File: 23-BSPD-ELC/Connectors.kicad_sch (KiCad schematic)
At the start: 11 parts, among them J1 Conn_02x06_Counter_Clockwise

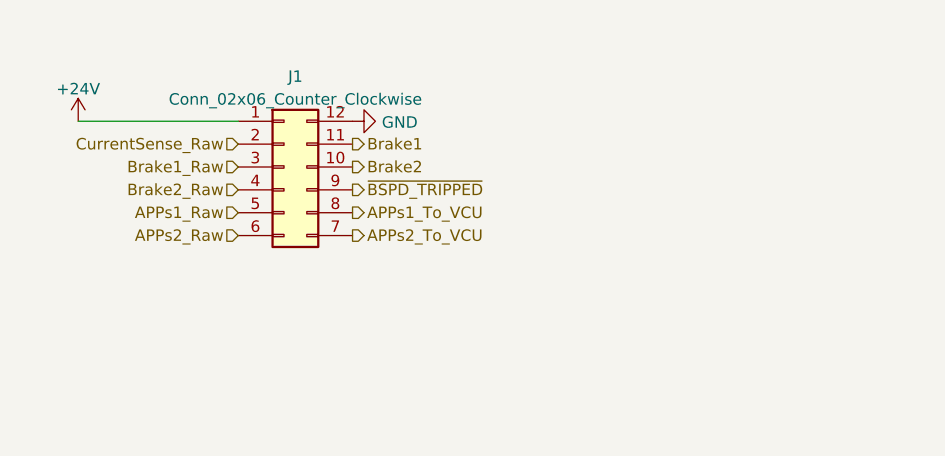
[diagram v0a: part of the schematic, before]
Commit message: Updated connectors and added ~brake signal to vcu
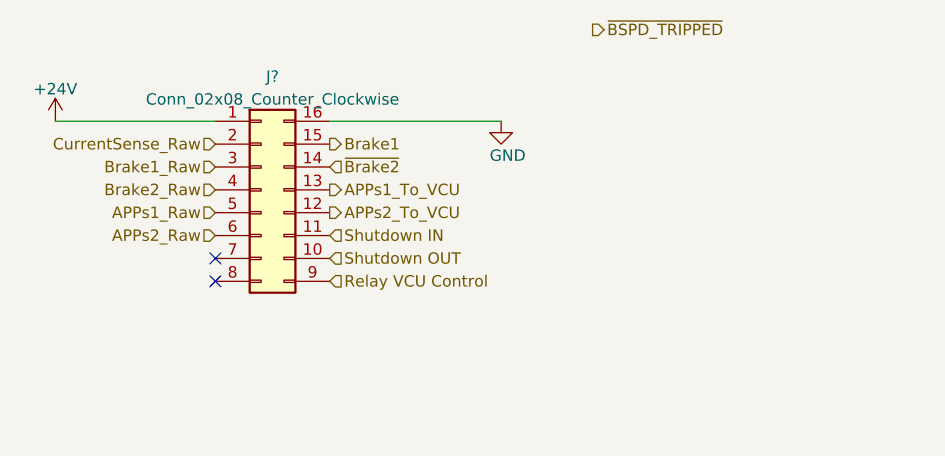
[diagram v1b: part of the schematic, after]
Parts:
- removed J1: Conn_02x06_Counter_Clockwise, symbol Connector_Generic:Conn_02x06_Counter_Clockwise
- added J?: Conn_02x08_Counter_Clockwise, symbol Connector_Generic:Conn_02x08_Counter_Clockwise
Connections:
- net +24V: now also J?.1 (Pin_1)
- net APPs1_Raw: now also J?.5 (Pin_5)
- net APPs1_To_VCU: now also J?.13 (Pin_13)
- net APPs2_Raw: now also J?.6 (Pin_6)
- net APPs2_To_VCU: now also J?.12 (Pin_12)
- net Brake1: now also J?.15 (Pin_15)
- net Brake1_Raw: now also J?.3 (Pin_3)
- net Brake2_Raw: now also J?.4 (Pin_4)
- net CurrentSense_Raw: now also J?.2 (Pin_2)
- net GND: now also J?.16 (Pin_16)
- new net Relay VCU Control: J?.9 (Pin_9)
- new net Shutdown IN: J?.11 (Pin_11)
- new net Shutdown OUT: J?.10 (Pin_10)
- new net ~{Brake2}: J?.14 (Pin_14)
- no-connect marks 4 -> 6
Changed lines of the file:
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@@
   (junction (at 187.96 88.9) (diameter 0) (color 0 0 0 0)
   )
+  (no_connect (at 67.31 100.33))
+  (no_connect (at 67.31 102.87))
   (no_connect (at 193.04 91.44))
   (no_connect (at 231.14 96.52))
@@
     (stroke (width 0) (type default) (color 0 0 0 0))
   )
+  (wire (pts (xy 80.01 85.09) (xy 99.06 85.09))
+    (stroke (width 0) (type default) (color 0 0 0 0))
+  )
   (wire (pts (xy 237.49 91.44) (xy 252.73 91.44))
     (stroke (width 0) (type default) (color 0 0 0 0))
@@
     (stroke (width 0) (type default) (color 0 0 0 0))
   )
-  (wire (pts (xy 52.07 85.09) (xy 69.85 85.09))
+  (wire (pts (xy 49.53 85.09) (xy 67.31 85.09))
     (stroke (width 0) (type default) (color 0 0 0 0))
   )
@@
     (stroke (width 0) (type default) (color 0 0 0 0))
   )
-  (hierarchical_label "APPs1_Raw" (shape input) (at 69.85 95.25 180)
-    (effects (font (size 1.27 1.27)) (justify right))
-  )
-  (hierarchical_label "Brake1_Raw" (shape input) (at 69.85 90.17 180)
-    (effects (font (size 1.27 1.27)) (justify right))
-  )
-  (hierarchical_label "APPs2_Raw" (shape input) (at 69.85 97.79 180)
-    (effects (font (size 1.27 1.27)) (justify right))
-  )
-  (hierarchical_label "Brake2" (shape output) (at 82.55 90.17 0)
-    (effects (font (size 1.27 1.27)) (justify left))
+  (hierarchical_label "APPs1_Raw" (shape input) (at 67.31 95.25 180)
+    (effects (font (size 1.27 1.27)) (justify right))
+  )
+  (hierarchical_label "Shutdown OUT" (shape input) (at 80.01 100.33 0)
+    (effects (font (size 1.27 1.27)) (justify left))
+  )
+  (hierarchical_label "Relay VCU Control" (shape input) (at 80.01 102.87 0)
+    (effects (font (size 1.27 1.27)) (justify left))
+  )
+  (hierarchical_label "Brake1_Raw" (shape input) (at 67.31 90.17 180)
+    (effects (font (size 1.27 1.27)) (justify right))
+  )
+  (hierarchical_label "APPs2_Raw" (shape input) (at 67.31 97.79 180)
+    (effects (font (size 1.27 1.27)) (justify right))
   )
   (hierarchical_label "Brake2_Raw" (shape input) (at 190.5 120.65 0)
@@
     (effects (font (size 1.27 1.27)) (justify left))
   )
-  (hierarchical_label "APPs1_To_VCU" (shape output) (at 82.55 95.25 0)
-    (effects (font (size 1.27 1.27)) (justify left))
-  )
-  (hierarchical_label "APPs2_To_VCU" (shape output) (at 82.55 97.79 0)
-    (effects (font (size 1.27 1.27)) (justify left))
-  )
-  (hierarchical_label "~{BSPD_TRIPPED}" (shape output) (at 82.55 92.71 0)
-    (effects (font (size 1.27 1.27)) (justify left))
-  )
-  (hierarchical_label "Brake1" (shape output) (at 82.55 87.63 0)
-    (effects (font (size 1.27 1.27)) (justify left))
-  )
-  (hierarchical_label "CurrentSense_Raw" (shape input) (at 69.85 87.63 180)
-    (effects (font (size 1.27 1.27)) (justify right))
-  )
-  (hierarchical_label "Brake2_Raw" (shape input) (at 69.85 92.71 180)
-    (effects (font (size 1.27 1.27)) (justify right))
-  )
-  (symbol (lib_id "power:GND") (at 82.55 85.09 90) (mirror x) (unit 1)
-    (in_bom yes) (on_board yes)
-    (property "Reference" "#PWR02" (id 0) (at 88.9 85.09 0)
-      (effects (font (size 1.27 1.27)) hide)
-    )
-    (property "Value" "GND" (id 1) (at 85.8012 85.217 90)
+  (hierarchical_label "APPs1_To_VCU" (shape output) (at 80.01 92.71 0)
+    (effects (font (size 1.27 1.27)) (justify left))
+  )
+  (hierarchical_label "APPs2_To_VCU" (shape output) (at 80.01 95.25 0)
+    (effects (font (size 1.27 1.27)) (justify left))
+  )
+  (hierarchical_label "~{BSPD_TRIPPED}" (shape output) (at 109.22 74.93 0)
+    (effects (font (size 1.27 1.27)) (justify left))
+  )
+  (hierarchical_label "Shutdown IN" (shape input) (at 80.01 97.79 0)
+    (effects (font (size 1.27 1.27)) (justify left))
+  )
+  (hierarchical_label "Brake1" (shape output) (at 80.01 87.63 0)
+    (effects (font (size 1.27 1.27)) (justify left))
+  )
+  (hierarchical_label "~{Brake2}" (shape input) (at 80.01 90.17 0)
+    (effects (font (size 1.27 1.27)) (justify left))
+  )
+  (hierarchical_label "CurrentSense_Raw" (shape input) (at 67.31 87.63 180)
+    (effects (font (size 1.27 1.27)) (justify right))
+  )
+  (hierarchical_label "Brake2_Raw" (shape input) (at 67.31 92.71 180)
+    (effects (font (size 1.27 1.27)) (justify right))
+  )
+  (symbol (lib_id "power:GND") (at 99.06 85.09 0) (mirror y) (unit 1)
+    (in_bom yes) (on_board yes)
+    (property "Reference" "#PWR02" (id 0) (at 99.06 91.44 0)
+      (effects (font (size 1.27 1.27)) hide)
+    )
+    (property "Value" "GND" (id 1) (at 97.79 88.9 0)
       (effects (font (size 1.27 1.27)) (justify right))
     )
-    (property "Footprint" "" (id 2) (at 82.55 85.09 0)
-      (effects (font (size 1.27 1.27)) hide)
-    )
-    (property "Datasheet" "" (id 3) (at 82.55 85.09 0)
+    (property "Footprint" "" (id 2) (at 99.06 85.09 0)
+      (effects (font (size 1.27 1.27)) hide)
+    )
+    (property "Datasheet" "" (id 3) (at 99.06 85.09 0)
       (effects (font (size 1.27 1.27)) hide)
     )
@@
     (pin "1")
   )
-  (symbol (lib_id "20-ELC-2-01-R1(Appetizer)-rescue:TestPoint-Connector") (at 237.49 91.44 0) (unit 1)
-    (in_bom yes) (on_board yes)
-    (property "Reference" "TP4" (id 0) (at 238.76 83.82 0)
-      (effects (font (size 1.27 1.27)) (justify left))
-    )
-    (property "Value" "TestPoint-Connector" (id 1) (at 237.49 86.36 0)
-      (effects (font (size 1.27 1.27)) (justify left))
-    )
-    (property "Footprint" "TestPoint:TestPoint_THTPad_D1.0mm_Drill0.5mm" (id 2) (at 242.57 91.44 0)
-      (effects (font (size 1.27 1.27)) hide)
-    )
-    (property "Datasheet" "" (id 3) (at 242.57 91.44 0)
-      (effects (font (size 1.27 1.27)) hide)
-    )
-    (pin "1")
-  )
-  (symbol (lib_id "20-ELC-2-01-R1(Appetizer)-rescue:TestPoint-Connector") (at 180.34 110.49 90) (unit 1)
-    (in_bom yes) (on_board yes)
-    (property "Reference" "TP1" (id 0) (at 166.37 109.22 90))
-    (property "Value" "TestPoint-Connector" (id 1) (at 166.37 111.76 90))
-    (property "Footprint" "TestPoint:TestPoint_THTPad_D1.0mm_Drill0.5mm" (id 2) (at 180.34 105.41 0)
-      (effects (font (size 1.27 1.27)) hide)
-    )
-    (property "Datasheet" "" (id 3) (at 180.34 105.41 0)
-      (effects (font (size 1.27 1.27)) hide)
-    )
-    (pin "1")
-  )
-  (symbol (lib_id "Connector_Generic:Conn_02x06_Counter_Clockwise") (at 74.93 90.17 0) (unit 1)
-    (in_bom yes) (on_board yes) (fields_autoplaced)
-    (property "Reference" "J1" (id 0) (at 76.2 80.1202 0))
-    (property "Value" "Conn_02x06_Counter_Clockwise" (id 1) (at 76.2 82.6571 0))
-    (property "Footprint" "" (id 2) (at 74.93 90.17 0)
-      (effects (font (size 1.27 1.27)) hide)
-    )
-    (property "Datasheet" "~" (id 3) (at 74.93 90.17 0)
+  (symbol (lib_id "Connector_Generic:Conn_02x08_Counter_Clockwise") (at 72.39 92.71 0) (unit 1)
+    (in_bom yes) (on_board yes) (fields_autoplaced)
+    (property "Reference" "J?" (id 0) (at 73.66 80.1202 0))
+    (property "Value" "Conn_02x08_Counter_Clockwise" (id 1) (at 73.66 82.6571 0))
+    (property "Footprint" "" (id 2) (at 72.39 92.71 0)
+      (effects (font (size 1.27 1.27)) hide)
+    )
+    (property "Datasheet" "~" (id 3) (at 72.39 92.71 0)
       (effects (font (size 1.27 1.27)) hide)
     )
@@
     (pin "11")
     (pin "12")
+    (pin "13")
+    (pin "14")
+    (pin "15")
+    (pin "16")
     (pin "2")
     (pin "3")
@@
     (pin "9")
   )
+  (symbol (lib_id "20-ELC-2-01-R1(Appetizer)-rescue:TestPoint-Connector") (at 237.49 91.44 0) (unit 1)
+    (in_bom yes) (on_board yes)
+    (property "Reference" "TP4" (id 0) (at 238.76 83.82 0)
+      (effects (font (size 1.27 1.27)) (justify left))
+    )
+    (property "Value" "TestPoint-Connector" (id 1) (at 237.49 86.36 0)
+      (effects (font (size 1.27 1.27)) (justify left))
+    )
+    (property "Footprint" "TestPoint:TestPoint_THTPad_D1.0mm_Drill0.5mm" (id 2) (at 242.57 91.44 0)
+      (effects (font (size 1.27 1.27)) hide)
+    )
+    (property "Datasheet" "" (id 3) (at 242.57 91.44 0)
+      (effects (font (size 1.27 1.27)) hide)
+    )
+    (pin "1")
+  )
+  (symbol (lib_id "20-ELC-2-01-R1(Appetizer)-rescue:TestPoint-Connector") (at 180.34 110.49 90) (unit 1)
+    (in_bom yes) (on_board yes)
+    (property "Reference" "TP1" (id 0) (at 166.37 109.22 90))
+    (property "Value" "TestPoint-Connector" (id 1) (at 166.37 111.76 90))
+    (property "Footprint" "TestPoint:TestPoint_THTPad_D1.0mm_Drill0.5mm" (id 2) (at 180.34 105.41 0)
+      (effects (font (size 1.27 1.27)) hide)
+    )
+    (property "Datasheet" "" (id 3) (at 180.34 105.41 0)
+      (effects (font (size 1.27 1.27)) hide)
+    )
+    (pin "1")
+  )
   (symbol (lib_id "20-ELC-2-01-R1(Appetizer)-rescue:TestPoint-Connector") (at 187.96 88.9 0) (unit 1)
     (in_bom yes) (on_board yes) (fields_autoplaced)
@@
     (pin "1")
   )
-  (symbol (lib_id "power:+24V") (at 52.07 85.09 0) (unit 1)
-    (in_bom yes) (on_board yes) (fields_autoplaced)
-    (property "Reference" "#PWR01" (id 0) (at 52.07 88.9 0)
-      (effects (font (size 1.27 1.27)) hide)
-    )
-    (property "Value" "+24V" (id 1) (at 52.07 81.5142 0))
-    (property "Footprint" "" (id 2) (at 52.07 85.09 0)
-      (effects (font (size 1.27 1.27)) hide)
-    )
-    (property "Datasheet" "" (id 3) (at 52.07 85.09 0)
-      (effects (font (size 1.27 1.27)) hide)
-    )
+  (symbol (lib_id "power:+24V") (at 49.53 85.09 0) (unit 1)
+    (in_bom yes) (on_board yes) (fields_autoplaced)
+    (property "Reference" "#PWR01" (id 0) (at 49.53 88.9 0)
+      (effects (font (size 1.27 1.27)) hide)
+    )
+    (property "Value" "+24V" (id 1) (at 49.53 81.5142 0))
+    (property "Footprint" "" (id 2) (at 49.53 85.09 0)
+      (effects (font (size 1.27 1.27)) hide)
+    )
+    (property "Datasheet" "" (id 3) (at 49.53 85.09 0)
+      (effects (font (size 1.27 1.27)) hide)
+    )

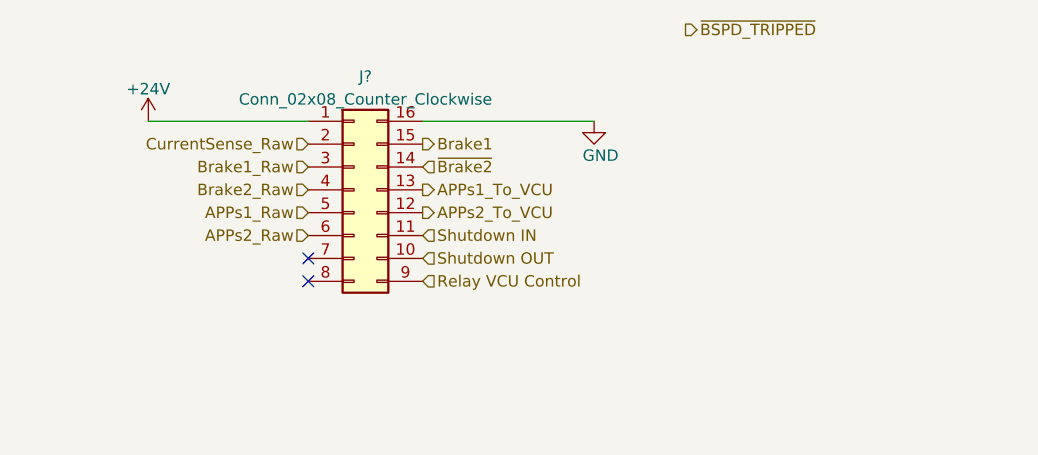
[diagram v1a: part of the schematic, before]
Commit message: Revision changes and updates to some footprints
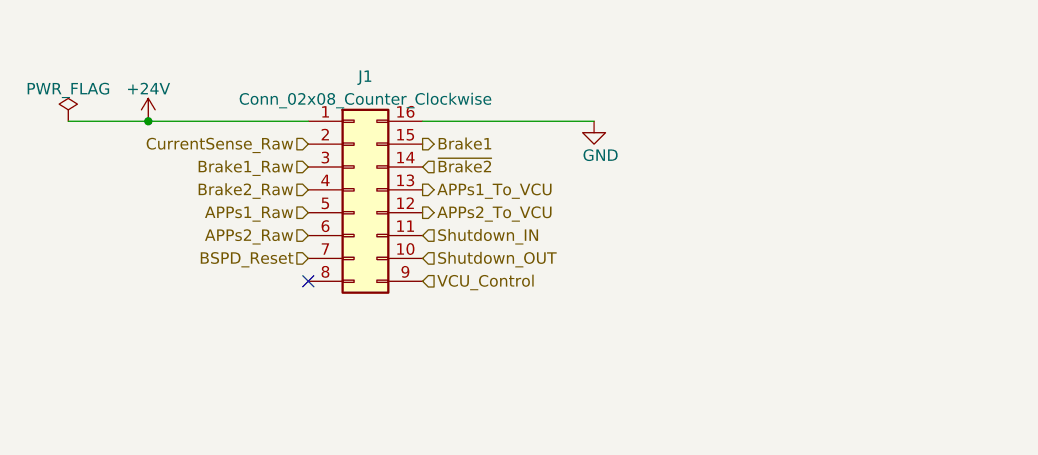
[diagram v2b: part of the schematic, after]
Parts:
- gave numbers to parts that had none: 1
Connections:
- net BSPD_Reset: now reaches J1.7 (Pin_7)
- net Relay VCU Control renamed VCU_Control
- net Shutdown IN renamed Shutdown_IN
- net Shutdown OUT renamed Shutdown_OUT
- no-connect marks 6 -> 5
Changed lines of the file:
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@@
   (junction (at 180.34 110.49) (diameter 0) (color 0 0 0 0)
   )
+  (junction (at 49.53 85.09) (diameter 0) (color 0 0 0 0)
+  )
   (junction (at 245.11 93.98) (diameter 0) (color 0 0 0 0)
   )
   (junction (at 187.96 88.9) (diameter 0) (color 0 0 0 0)
   )
-  (no_connect (at 67.31 100.33))
   (no_connect (at 67.31 102.87))
   (no_connect (at 193.04 91.44))
@@
     (stroke (width 0) (type default) (color 0 0 0 0))
   )
+  (wire (pts (xy 40.64 85.09) (xy 49.53 85.09))
+    (stroke (width 0) (type default) (color 0 0 0 0))
+  )
   (wire (pts (xy 182.88 88.9) (xy 187.96 88.9))
     (stroke (width 0) (type default) (color 0 0 0 0))
@@
     (stroke (width 0) (type default) (color 0 0 0 0))
   )
+  (wire (pts (xy 190.5 99.06) (xy 190.5 109.22))
+    (stroke (width 0) (type default) (color 0 0 0 0))
+  )
+  (wire (pts (xy 180.34 96.52) (xy 180.34 110.49))
+    (stroke (width 0) (type default) (color 0 0 0 0))
+  )
+  (wire (pts (xy 190.5 109.22) (xy 190.5 120.65))
+    (stroke (width 0) (type default) (color 0 0 0 0))
+  )
+  (wire (pts (xy 231.14 93.98) (xy 245.11 93.98))
+    (stroke (width 0) (type default) (color 0 0 0 0))
+  )
+  (wire (pts (xy 231.14 91.44) (xy 237.49 91.44))
+    (stroke (width 0) (type default) (color 0 0 0 0))
+  )
+  (wire (pts (xy 172.72 93.98) (xy 193.04 93.98))
+    (stroke (width 0) (type default) (color 0 0 0 0))
+  )
   (wire (pts (xy 49.53 85.09) (xy 67.31 85.09))
     (stroke (width 0) (type default) (color 0 0 0 0))
   )
-  (wire (pts (xy 190.5 99.06) (xy 190.5 109.22))
-    (stroke (width 0) (type default) (color 0 0 0 0))
-  )
-  (wire (pts (xy 180.34 96.52) (xy 180.34 110.49))
-    (stroke (width 0) (type default) (color 0 0 0 0))
-  )
-  (wire (pts (xy 190.5 109.22) (xy 190.5 120.65))
-    (stroke (width 0) (type default) (color 0 0 0 0))
-  )
-  (wire (pts (xy 231.14 93.98) (xy 245.11 93.98))
-    (stroke (width 0) (type default) (color 0 0 0 0))
-  )
-  (wire (pts (xy 231.14 91.44) (xy 237.49 91.44))
-    (stroke (width 0) (type default) (color 0 0 0 0))
-  )
-  (wire (pts (xy 172.72 93.98) (xy 193.04 93.98))
-    (stroke (width 0) (type default) (color 0 0 0 0))
-  )
   (hierarchical_label "APPs1_Raw" (shape input) (at 67.31 95.25 180)
     (effects (font (size 1.27 1.27)) (justify right))
   )
-  (hierarchical_label "Shutdown OUT" (shape input) (at 80.01 100.33 0)
-    (effects (font (size 1.27 1.27)) (justify left))
-  )
-  (hierarchical_label "Relay VCU Control" (shape input) (at 80.01 102.87 0)
+  (hierarchical_label "Shutdown_OUT" (shape input) (at 80.01 100.33 0)
     (effects (font (size 1.27 1.27)) (justify left))
   )
@@
     (effects (font (size 1.27 1.27)) (justify right))
   )
+  (hierarchical_label "VCU_Control" (shape input) (at 80.01 102.87 0)
+    (effects (font (size 1.27 1.27)) (justify left))
+  )
   (hierarchical_label "APPs2_Raw" (shape input) (at 67.31 97.79 180)
     (effects (font (size 1.27 1.27)) (justify right))
@@
     (effects (font (size 1.27 1.27)) (justify left))
   )
-  (hierarchical_label "~{BSPD_TRIPPED}" (shape output) (at 109.22 74.93 0)
-    (effects (font (size 1.27 1.27)) (justify left))
-  )
-  (hierarchical_label "Shutdown IN" (shape input) (at 80.01 97.79 0)
+  (hierarchical_label "BSPD_Reset" (shape input) (at 67.31 100.33 180)
+    (effects (font (size 1.27 1.27)) (justify right))
+  )
+  (hierarchical_label "Shutdown_IN" (shape input) (at 80.01 97.79 0)
     (effects (font (size 1.27 1.27)) (justify left))
   )
@@
   (symbol (lib_id "Connector_Generic:Conn_02x08_Counter_Clockwise") (at 72.39 92.71 0) (unit 1)
     (in_bom yes) (on_board yes) (fields_autoplaced)
-    (property "Reference" "J?" (id 0) (at 73.66 80.1202 0))
+    (property "Reference" "J1" (id 0) (at 73.66 80.1202 0))
     (property "Value" "Conn_02x08_Counter_Clockwise" (id 1) (at 73.66 82.6571 0))
     (property "Footprint" "" (id 2) (at 72.39 92.71 0)
@@
     (pin "9")
   )
+  (symbol (lib_id "power:PWR_FLAG") (at 40.64 85.09 0) (unit 1)
+    (in_bom yes) (on_board yes) (fields_autoplaced)
+    (property "Reference" "#FLG01" (id 0) (at 40.64 83.185 0)
+      (effects (font (size 1.27 1.27)) hide)
+    )
+    (property "Value" "PWR_FLAG" (id 1) (at 40.64 81.5142 0))
+    (property "Footprint" "" (id 2) (at 40.64 85.09 0)
+      (effects (font (size 1.27 1.27)) hide)
+    )
+    (property "Datasheet" "~" (id 3) (at 40.64 85.09 0)
+      (effects (font (size 1.27 1.27)) hide)
+    )
+    (pin "1")
+  )
   (symbol (lib_id "20-ELC-2-01-R1(Appetizer)-rescue:TestPoint-Connector") (at 237.49 91.44 0) (unit 1)
